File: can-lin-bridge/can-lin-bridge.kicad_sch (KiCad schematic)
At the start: 0 parts

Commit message: can-lin-bridge: Add LIN transceiver (TJA1029)
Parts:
- added U1: TJA1029TK/20/1J, Package_DFN_QFN:DFN-8-1EP_3x3mm_P0.65mm_EP1.55x2.4mm, symbol Interface_CAN_LIN:TJA1029TK
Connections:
- new net +5V: U1.7 (VBAT)
- new net GND: U1.5 (GND), U1.9 (GND)
- new net LIN: U1.6 (LIN)
- new net LIN_RX: U1.1 (RXD)
- new net LIN_TX: U1.4 (TXD)
- new net ~{LIN_SLP}: U1.2 (~{SLP})

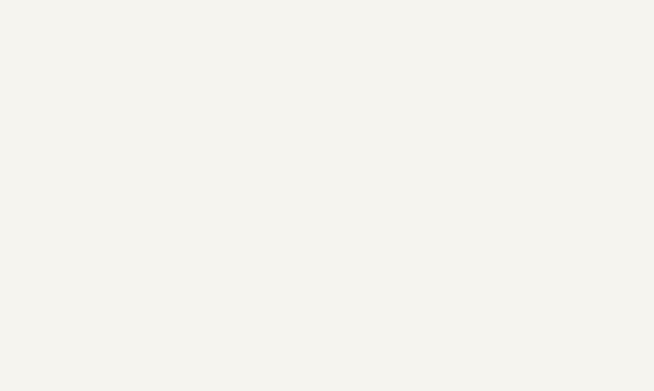
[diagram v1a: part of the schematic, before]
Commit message: can-lin-bridge: Add CAN transceiver (TJA1024)
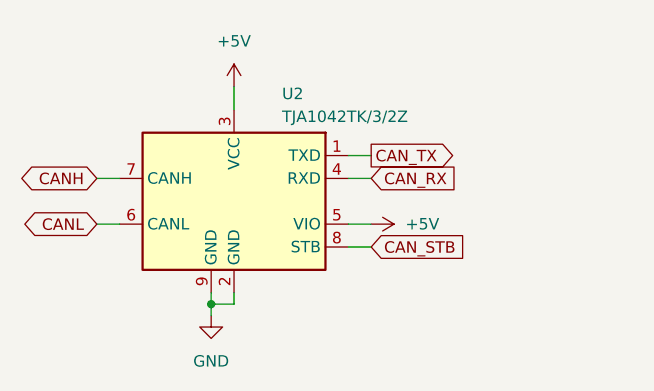
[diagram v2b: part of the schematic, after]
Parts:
- added U2: TJA1042TK/3/2Z, Package_DFN_QFN:DFN-8-1EP_3x3mm_P0.65mm_EP1.55x2.4mm, symbol Interface_CAN_LIN:TJA1042TK-3
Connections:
- net +5V: now also U2.3 (VCC), U2.5 (VIO)
- net GND: now also U2.2 (GND), U2.9 (GND)
- new net CANH: U2.7 (CANH)
- new net CANL: U2.6 (CANL)
- new net CAN_RX: U2.4 (RXD)
- new net CAN_STB: U2.8 (STB)
- new net CAN_TX: U2.1 (TXD)

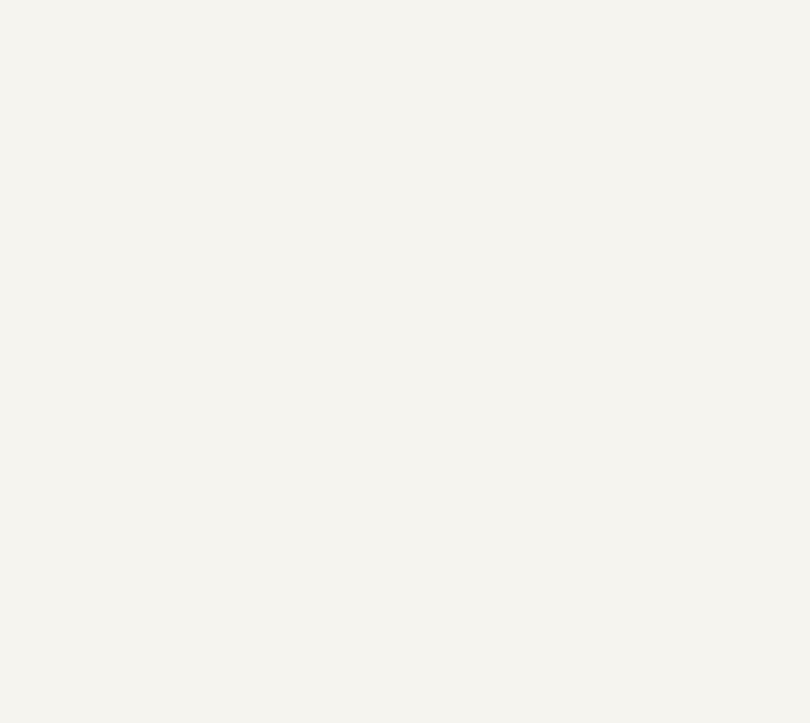
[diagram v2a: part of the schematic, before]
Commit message: can-lin-bridge: Add MCU to schematic (no connections yet)
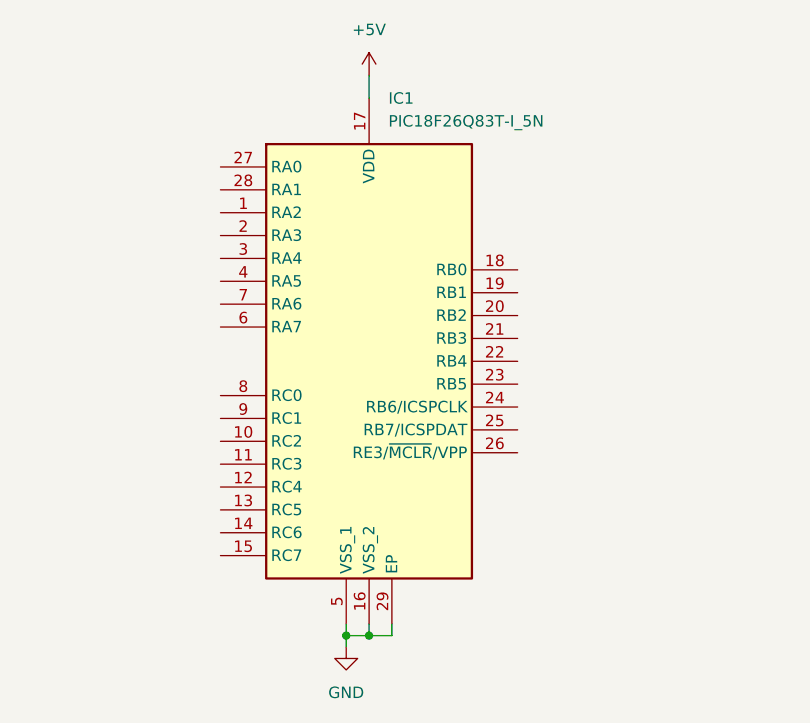
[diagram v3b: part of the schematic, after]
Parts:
- added IC1: PIC18F26Q83T-I_5N, QFN65P600X600X100-29N-D, symbol PIC18F26Q83T-I5N:PIC18F26Q83T-I_5N
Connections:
- net +5V: now also IC1.17 (VDD)
- net GND: now also IC1.16 (VSS_2), IC1.29 (EP), IC1.5 (VSS_1)

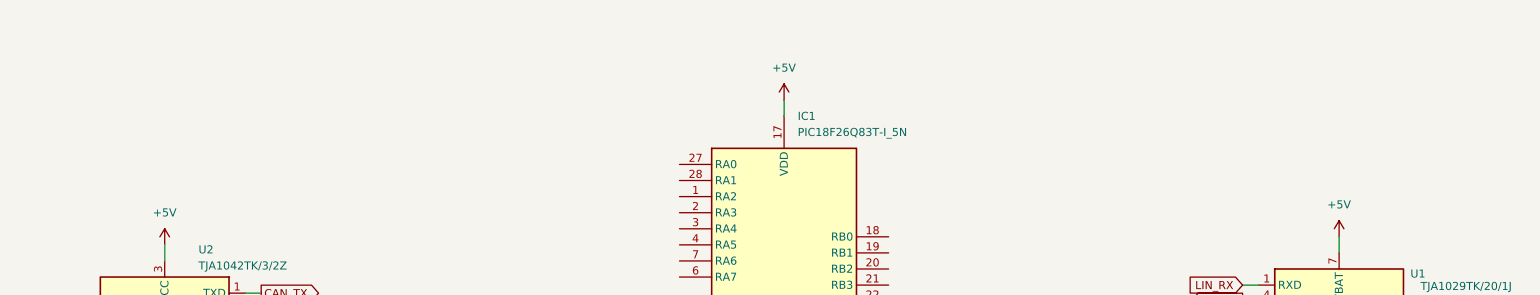
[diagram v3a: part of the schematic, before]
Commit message: can-lin-bridge: Add labels to schematic
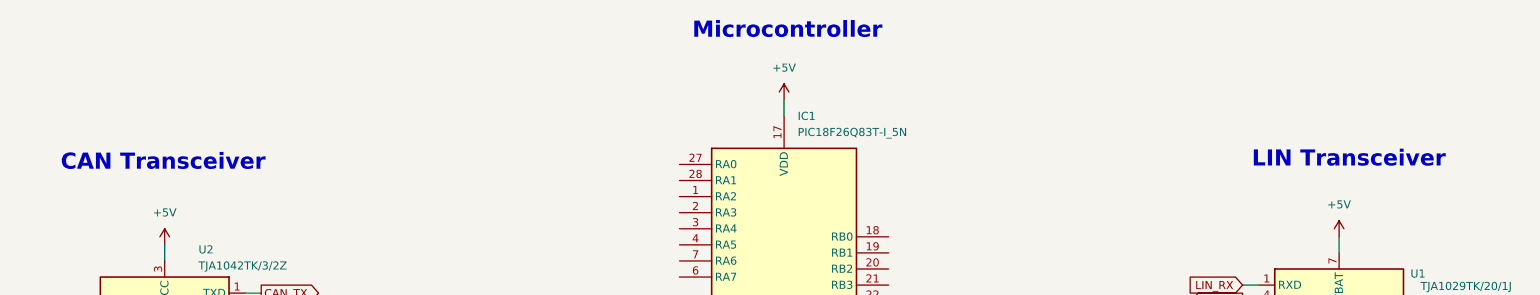
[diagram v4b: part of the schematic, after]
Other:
- note added: "CAN Transceiver"
- note added: "LIN Transceiver"
- note added: "Microcontroller"
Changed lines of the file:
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@@
 	(generator_version "9.0")
 	(paper "A4")
+	(text "LIN Transceiver"
+		(exclude_from_sim no)
+		(at 244.094 70.358 0)
+		(effects
+			(font
+				(size 2.54 2.54)
+				(thickness 0.508)
+				(bold yes)
+			)
+		)
+	)
+	(text "CAN Transceiver"
+		(exclude_from_sim no)
+		(at 56.896 70.866 0)
+		(effects
+			(font
+				(size 2.54 2.54)
+				(thickness 0.508)
+				(bold yes)
+			)
+		)
+	)
+	(text "Microcontroller"
+		(exclude_from_sim no)
+		(at 155.448 50.038 0)
+		(effects
+			(font
+				(size 2.54 2.54)
+				(thickness 0.508)
+				(bold yes)
+			)
+		)
+	)
 	(junction
 		(at 154.94 123.19)

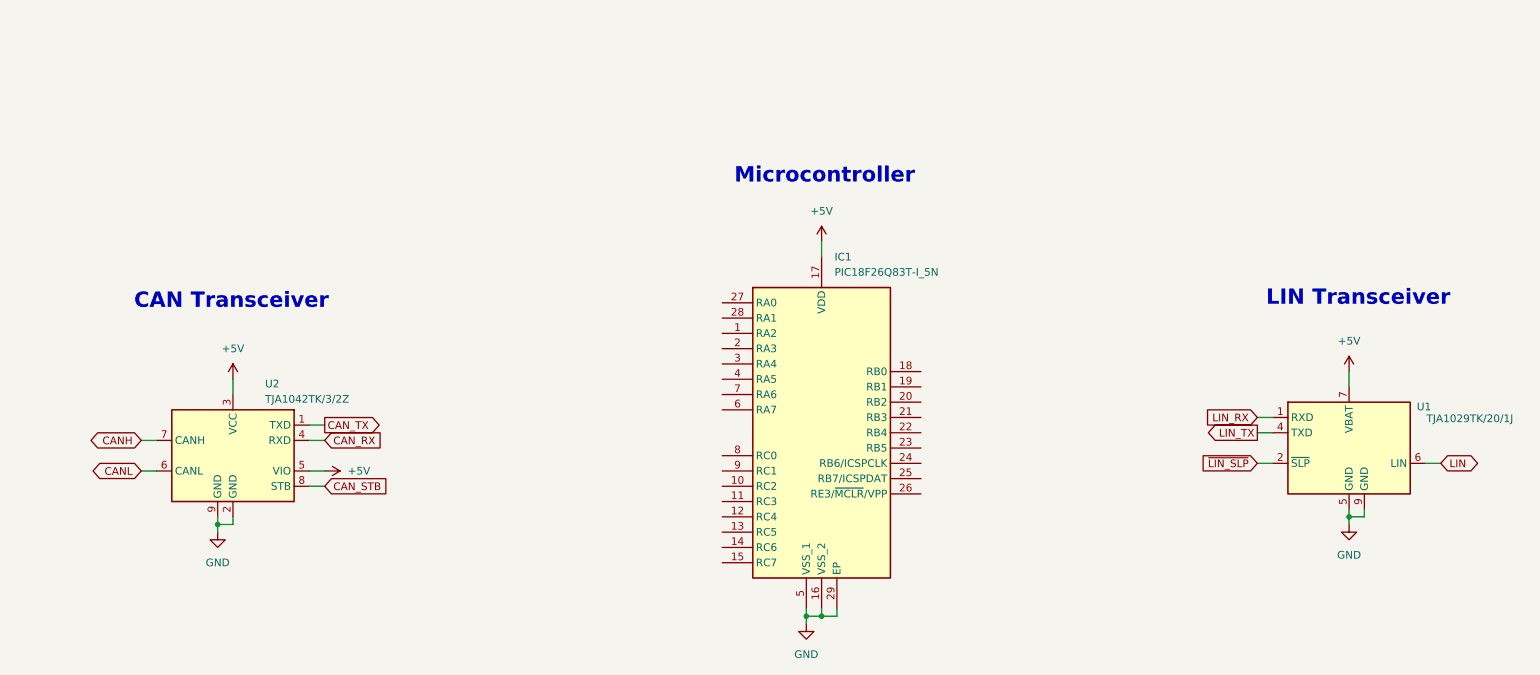
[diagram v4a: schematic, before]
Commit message: can-lin-bridge: Add decoupling capacitors for all ICs
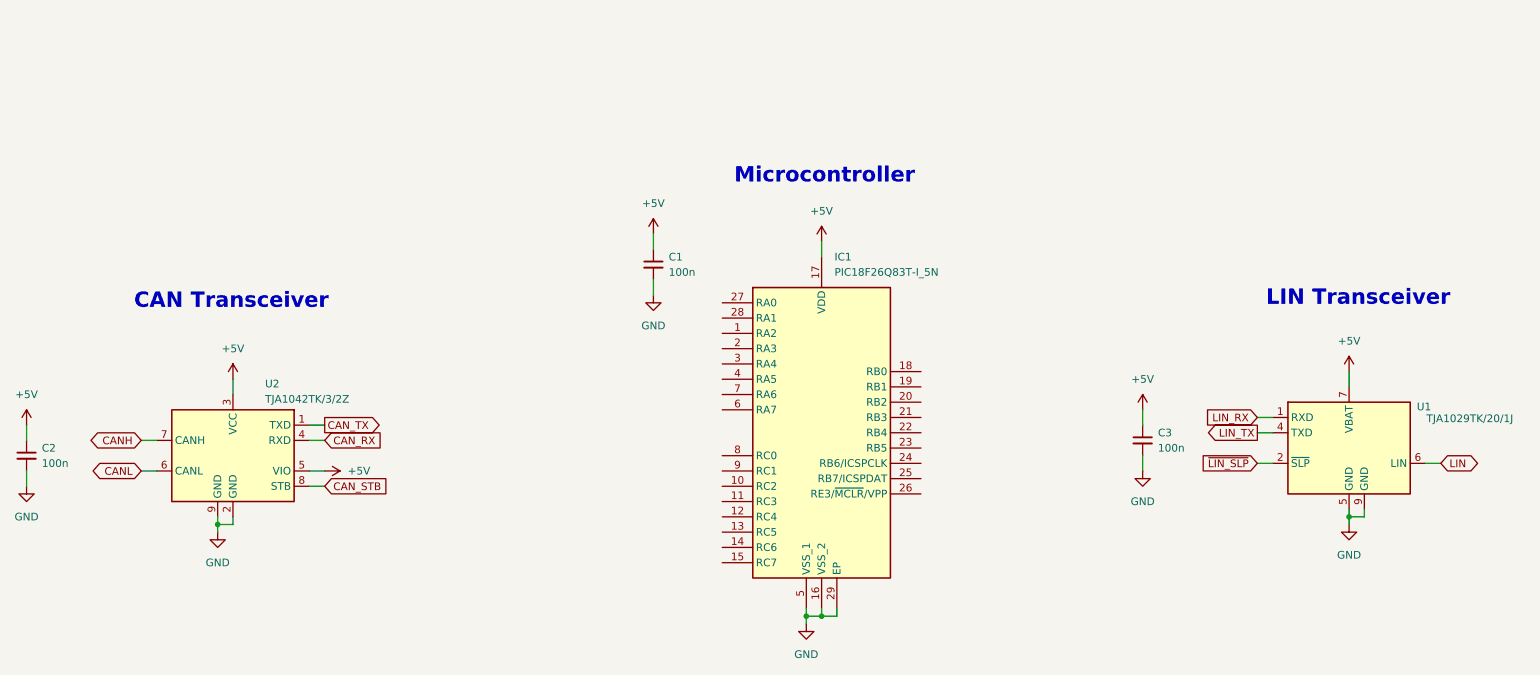
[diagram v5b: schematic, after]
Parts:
- added C1, C2, C3: 100n, symbol Device:C_Small
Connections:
- net +5V: now also C1.1, C2.1, C3.1
- net GND: now also C1.2, C2.2, C3.2

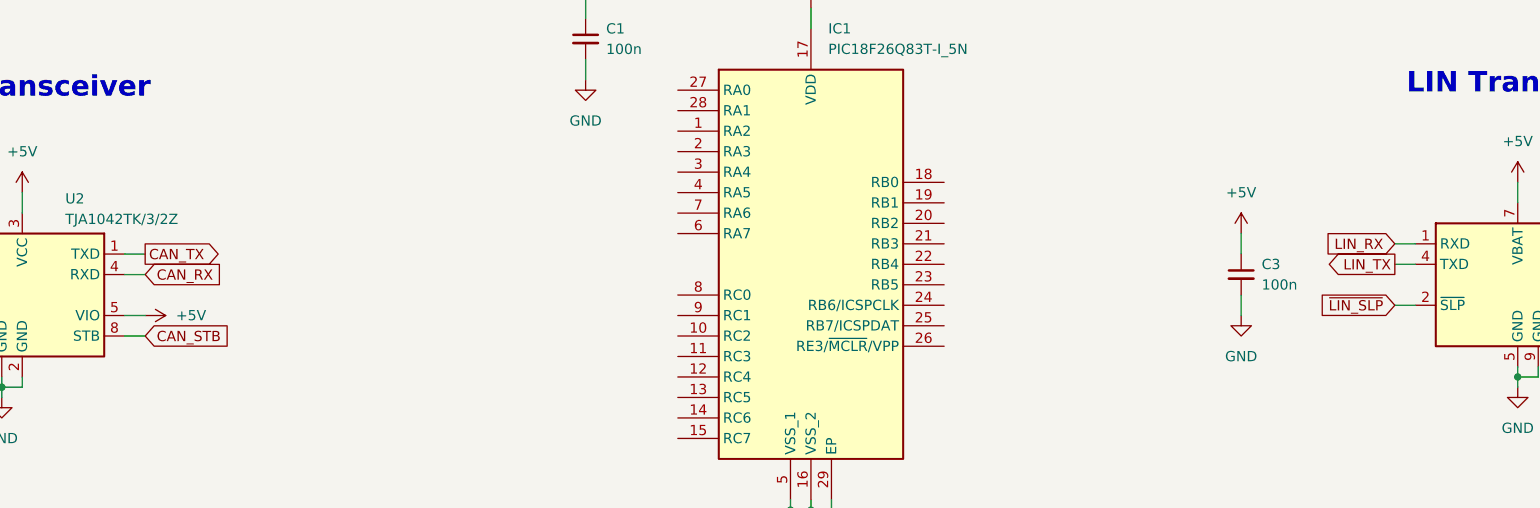
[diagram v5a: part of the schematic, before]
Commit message: can-lin-bridge: Connect CAN and LIN transceivers to the microcontroller
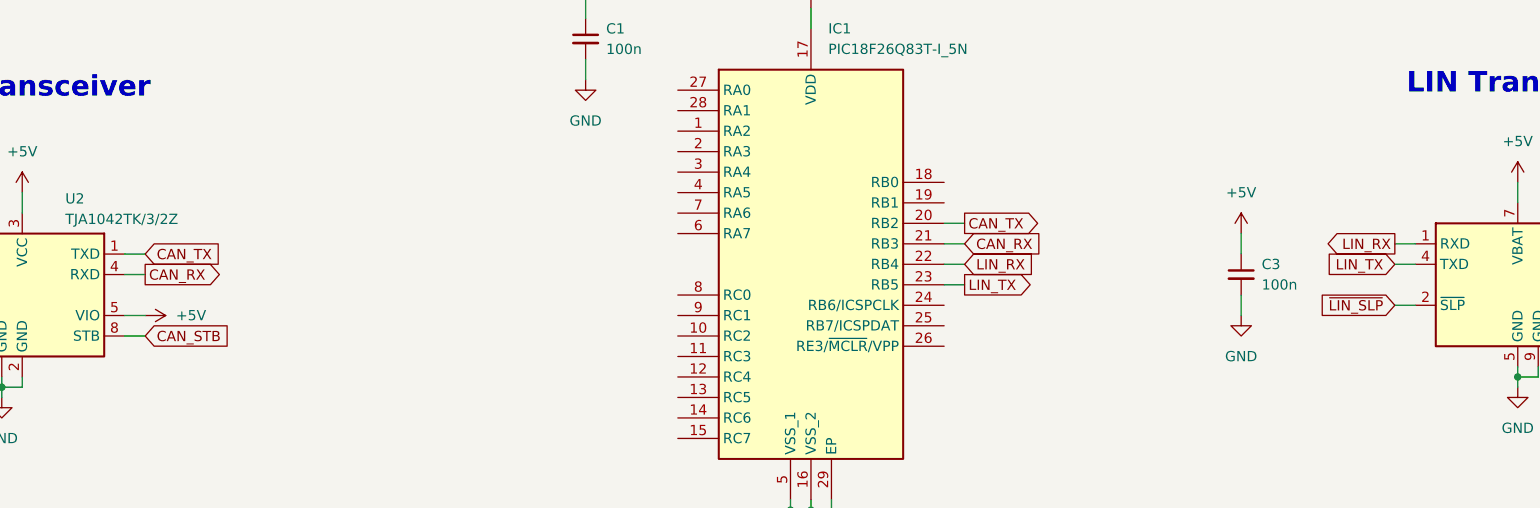
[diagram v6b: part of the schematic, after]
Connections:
- net CAN_RX: now also IC1.21 (RB3)
- net CAN_TX: now also IC1.20 (RB2)
- net LIN_RX: now also IC1.22 (RB4)
- net LIN_TX: now also IC1.23 (RB5)
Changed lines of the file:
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@@
+	(wire
+		(pts
+			(xy 171.45 90.17) (xy 173.99 90.17)
+		)
+		(stroke
+			(width 0)
+			(type default)
+		)
+	)
 	(wire
 		(pts
@@
 	(wire
 		(pts
+			(xy 171.45 92.71) (xy 173.99 92.71)
+		)
+		(stroke
+			(width 0)
+			(type default)
+		)
+	)
+	(wire
+		(pts
 			(xy 127 59.69) (xy 127 62.23)
 		)
@@
 	(wire
 		(pts
+			(xy 171.45 87.63) (xy 173.99 87.63)
+		)
+		(stroke
+			(width 0)
+			(type default)
+		)
+	)
+	(wire
+		(pts
 			(xy 57.15 83.82) (xy 57.15 86.36)
 		)
@@
 	(wire
 		(pts
+			(xy 171.45 95.25) (xy 173.99 95.25)
+		)
+		(stroke
+			(width 0)
+			(type default)
+		)
+	)
+	(wire
+		(pts
 			(xy 227.33 97.79) (xy 229.87 97.79)
 		)
@@
 			(width 0)
 			(type default)
+		)
+	)
+	(global_label "LIN_TX"
+		(shape output)
+		(at 173.99 95.25 0)
+		(fields_autoplaced yes)
+		(effects
+			(font
+				(size 1.27 1.27)
+			)
+			(justify left)
+		)
+		(property "Intersheetrefs" "${INTERSHEET_REFS}"
+			(at 183.0833 95.25 0)
+			(effects
+				(font
+					(size 1.27 1.27)
+				)
+				(justify left)
+				(hide yes)
+			)
 		)
 	)
@@
 		)
 	)
+	(global_label "LIN_RX"
+		(shape input)
+		(at 173.99 92.71 0)
+		(fields_autoplaced yes)
+		(effects
+			(font
+				(size 1.27 1.27)
+			)
+			(justify left)
+		)
+		(property "Intersheetrefs" "${INTERSHEET_REFS}"
+			(at 183.3857 92.71 0)
+			(effects
+				(font
+					(size 1.27 1.27)
+				)
+				(justify left)
+				(hide yes)
+			)
+		)
+	)
 	(global_label "~{LIN_SLP}"
 		(shape input)
@@
 	)
 	(global_label "CAN_RX"
+		(shape output)
+		(at 72.39 93.98 0)
+		(fields_autoplaced yes)
+		(effects
+			(font
+				(size 1.27 1.27)
+			)
+			(justify left)
+		)
+		(property "Intersheetrefs" "${INTERSHEET_REFS}"
+			(at 82.5114 93.98 0)
+			(effects
+				(font
+					(size 1.27 1.27)
+				)
+				(justify left)
+				(hide yes)
+			)
+		)
+	)
+	(global_label "CAN_TX"
+		(shape output)
+		(at 173.99 87.63 0)
+		(fields_autoplaced yes)
+		(effects
+			(font
+				(size 1.27 1.27)
+			)
+			(justify left)
+		)
+		(property "Intersheetrefs" "${INTERSHEET_REFS}"
+			(at 183.809 87.63 0)
+			(effects
+				(font
+					(size 1.27 1.27)
+				)
+				(justify left)
+				(hide yes)
+			)
+		)
+	)
+	(global_label "LIN_TX"
 		(shape input)
-		(at 72.39 93.98 0)
-		(fields_autoplaced yes)
-		(effects
-			(font
-				(size 1.27 1.27)
-			)
-			(justify left)
-		)
-		(property "Intersheetrefs" "${INTERSHEET_REFS}"
-			(at 82.5114 93.98 0)
-			(effects
-				(font
-					(size 1.27 1.27)
-				)
-				(justify left)
-				(hide yes)
-			)
-		)
-	)
-	(global_label "LIN_TX"
+		(at 227.33 92.71 180)
+		(fields_autoplaced yes)
+		(effects
+			(font
+				(size 1.27 1.27)
+			)
+			(justify right)
+		)
+		(property "Intersheetrefs" "${INTERSHEET_REFS}"
+			(at 218.2367 92.71 0)
+			(effects
+				(font
+					(size 1.27 1.27)
+				)
+				(justify right)
+				(hide yes)
+			)
+		)
+	)
+	(global_label "LIN_RX"
 		(shape output)
-		(at 227.33 92.71 180)
+		(at 227.33 90.17 180)
 		(fields_autoplaced yes)
 		(effects
@@
 		)
 		(property "Intersheetrefs" "${INTERSHEET_REFS}"
-			(at 218.2367 92.71 0)
+			(at 217.9343 90.17 0)
 			(effects
 				(font
@@
 		)
 	)
-	(global_label "LIN_RX"
+	(global_label "CAN_RX"
 		(shape input)
-		(at 227.33 90.17 180)
-		(fields_autoplaced yes)
-		(effects
-			(font
-				(size 1.27 1.27)
-			)
-			(justify right)
-		)
-		(property "Intersheetrefs" "${INTERSHEET_REFS}"
-			(at 217.9343 90.17 0)
-			(effects
-				(font
-					(size 1.27 1.27)
-				)
-				(justify right)
+		(at 173.99 90.17 0)
+		(fields_autoplaced yes)
+		(effects
+			(font
+				(size 1.27 1.27)
+			)
+			(justify left)
+		)
+		(property "Intersheetrefs" "${INTERSHEET_REFS}"
+			(at 184.1114 90.17 0)
+			(effects
+				(font
+					(size 1.27 1.27)
+				)
+				(justify left)
 				(hide yes)
 			)
@@
 	)
 	(global_label "CAN_TX"
-		(shape output)
+		(shape input)
 		(at 72.39 91.44 0)
 		(fields_autoplaced yes)

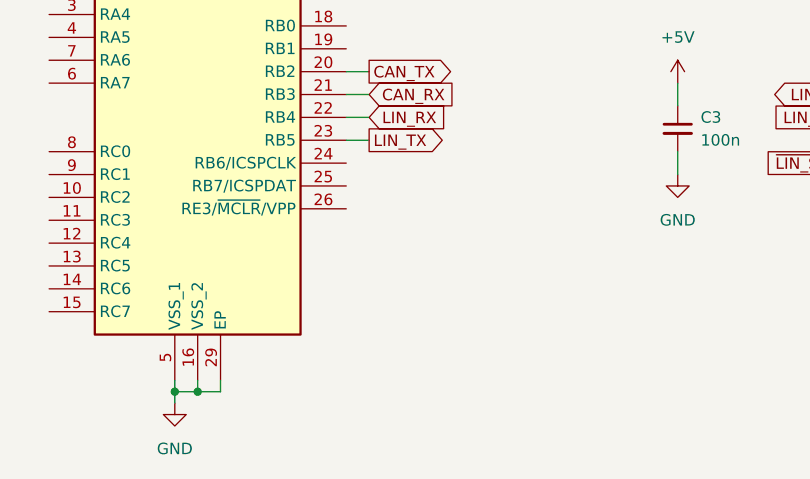
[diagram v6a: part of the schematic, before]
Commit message: can-lin-bridge: Add ICSP programmer header
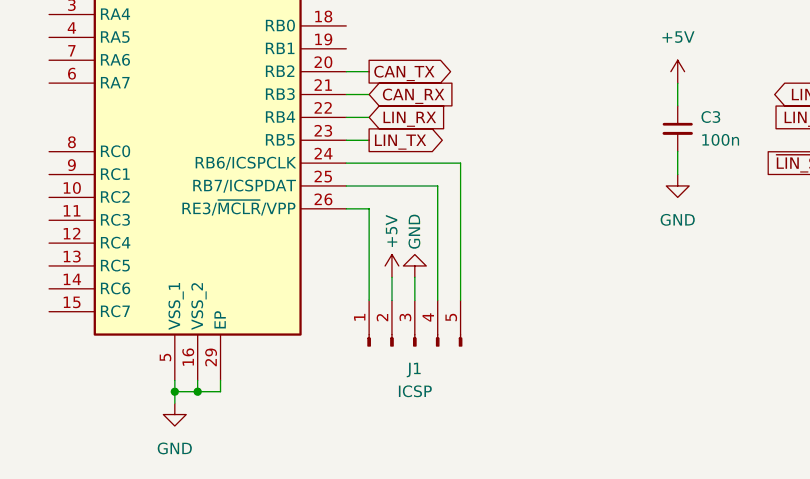
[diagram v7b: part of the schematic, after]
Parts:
- added J1: ICSP, symbol Connector:Conn_01x05_Pin
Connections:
- net +5V: now also J1.2 (Pin_2)
- net GND: now also J1.3 (Pin_3)
- net at IC1.24 (RB6/ICSPCLK): now also J1.5 (Pin_5)
- net at IC1.25 (RB7/ICSPDAT): now also J1.4 (Pin_4)
- net at IC1.26 (RE3/~{MCLR}/VPP): now also J1.1 (Pin_1)
